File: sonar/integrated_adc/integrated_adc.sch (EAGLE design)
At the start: 0 parts

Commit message: Largely done schematic.
Still to do:
- Teensy-style connections
- Analog connections
- Remember what else I'm forgetting.
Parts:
- added C1, C2: 22pF, resistor:C-EUC0805
- added C10, C11, C12, C13, C3, C4, C5, C6, C7, C8, C9: 0u1, resistor:C-EUC0805
- added C14: 4u7, resistor:C-EUC0805
- added C15: 10n, resistor:C-EUC0805
- added C16: 1u, resistor:C-EUC0805
- added CON1, CON2: UAVCAN_MICRO, integrated_adc:UAVCAN_MICRO
- added JP1: CORTEX-M-DBG, integrated_adc:CORTEX-M-DBG
- added R1: 10K, resistor:R-EU_R0805
- added U$1: MCP3021, integrated_adc:MCP3021
- added U$2: MCP2562-E/SN, integrated_adc:MCP2562-E/SN
- added U1: STM32F303RX, integrated_adc:STM32F303RX
- added Y1: NX5032, integrated_adc:NX5032
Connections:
- new net !RST: JP1.!RESET, R1.1, U1G$5.NRST
- new net +3V3: C10.1, C11.1, C12.1, C13.1, C14.1, C3.1, C4.1, C5.1, C6.1, C7.1, C8.1, C9.1, JP1.VCC, R1.2, U$2.VDD, U$2.VIO, U1G$5.VDD
- new net +3V3_CLEAN: C15.1, C16.1, U$1.VDD, U1G$5.VDDA
- new net ADC1: U1G$1.PA0
- new net ADC2: U1G$1.PA4
- new net ADC3: U1G$2.PB13
- new net ADC4: U1G$2.PB14
- new net CAN_RX: U$2.RXD, U1G$1.PA11
- new net CAN_TX: U$2.TXD, U1G$1.PA12
- new net GND: C1.2, C10.2, C11.2, C12.2, C13.2, C14.2, C2.2, C3.2, C4.2, C5.2, C6.2, C7.2, C8.2, C9.2, JP1.GND_1, JP1.GND_2, JP1.GND_DETECT, U$2.STBY, U$2.VSS, U1G$5.BOOT0, U1G$5.VSS
- new net GNDA: C15.2, C16.2, U$1.VSS, U1G$5.VSSA
- new net I2C2_SCL: U1G$1.PA9
- new net I2C2_SDA: U1G$1.PA10
- new net N$1: C1.1, U1G$5.PF0/OSC-IN, Y1.2
- new net N$2: C2.1, U1G$5.PF1/OSC-OUT, Y1.1
- new net N$3: CON1.CANH, CON2.CANH, U$2.CANH
- new net N$4: CON1.CANL, CON2.CANL, U$2.CANL
- new net N$5: CON1.+5V, CON2.+5V
- new net N$6: CON1.GND, CON1.TABS, CON2.GND, CON2.TABS
- new net SCL: U$1.SCL
- new net SDA: U$1.SDA
- new net SWCLK: JP1.SWCLK/TCK
- new net SWDCLK: U1G$1.PA14
- new net SWDIO: JP1.SWDIO/TMS, U1G$1.PA13
- new net TRACESWO: JP1.SWO/TDO, U1G$2.PB3
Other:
- note added: "12MHz"
- note added: "22pF loading capacitors not verified for 12MHz!"
- note added: "ADC1_IN1"
- note added: "ADC2_IN1"
- note added: "ADC3_IN5"
- note added: "ADC4_IN4"
- note added: "CAN Bus"
- note added: "Clock and Power"
- note added: "Debug Header"
- note added: "Decoupling"
- note added: "External ADC"
- note added: "Pin Assignments"

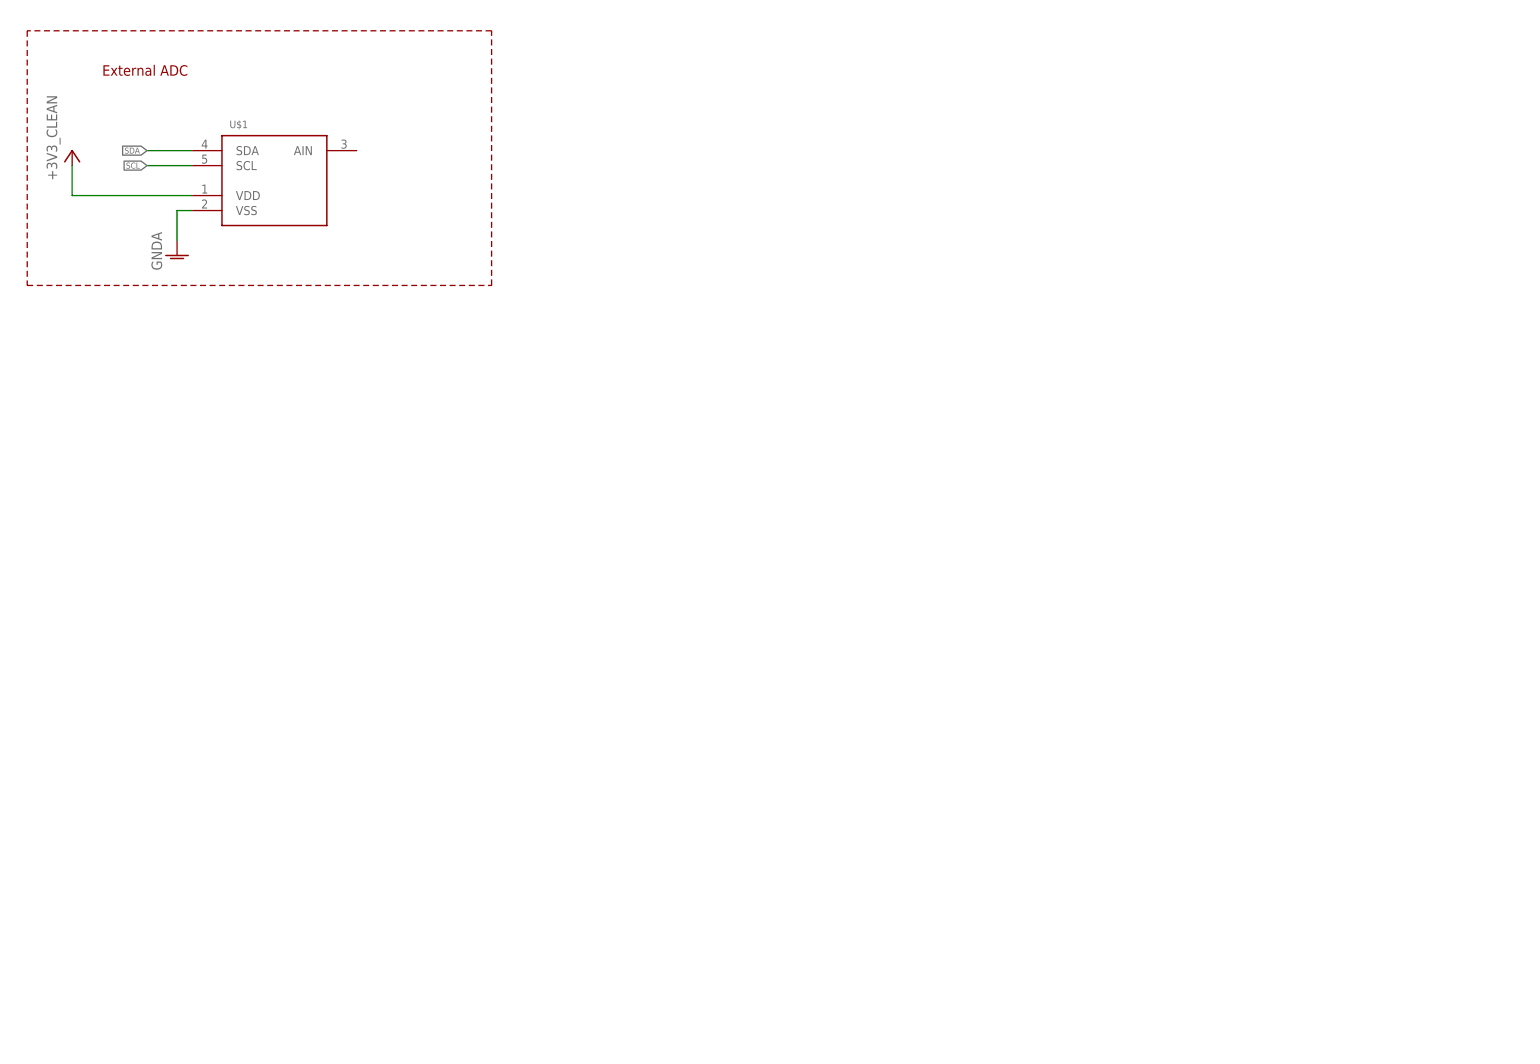
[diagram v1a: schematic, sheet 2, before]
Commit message: Switched to LQFP100 STM32 and added some headers.
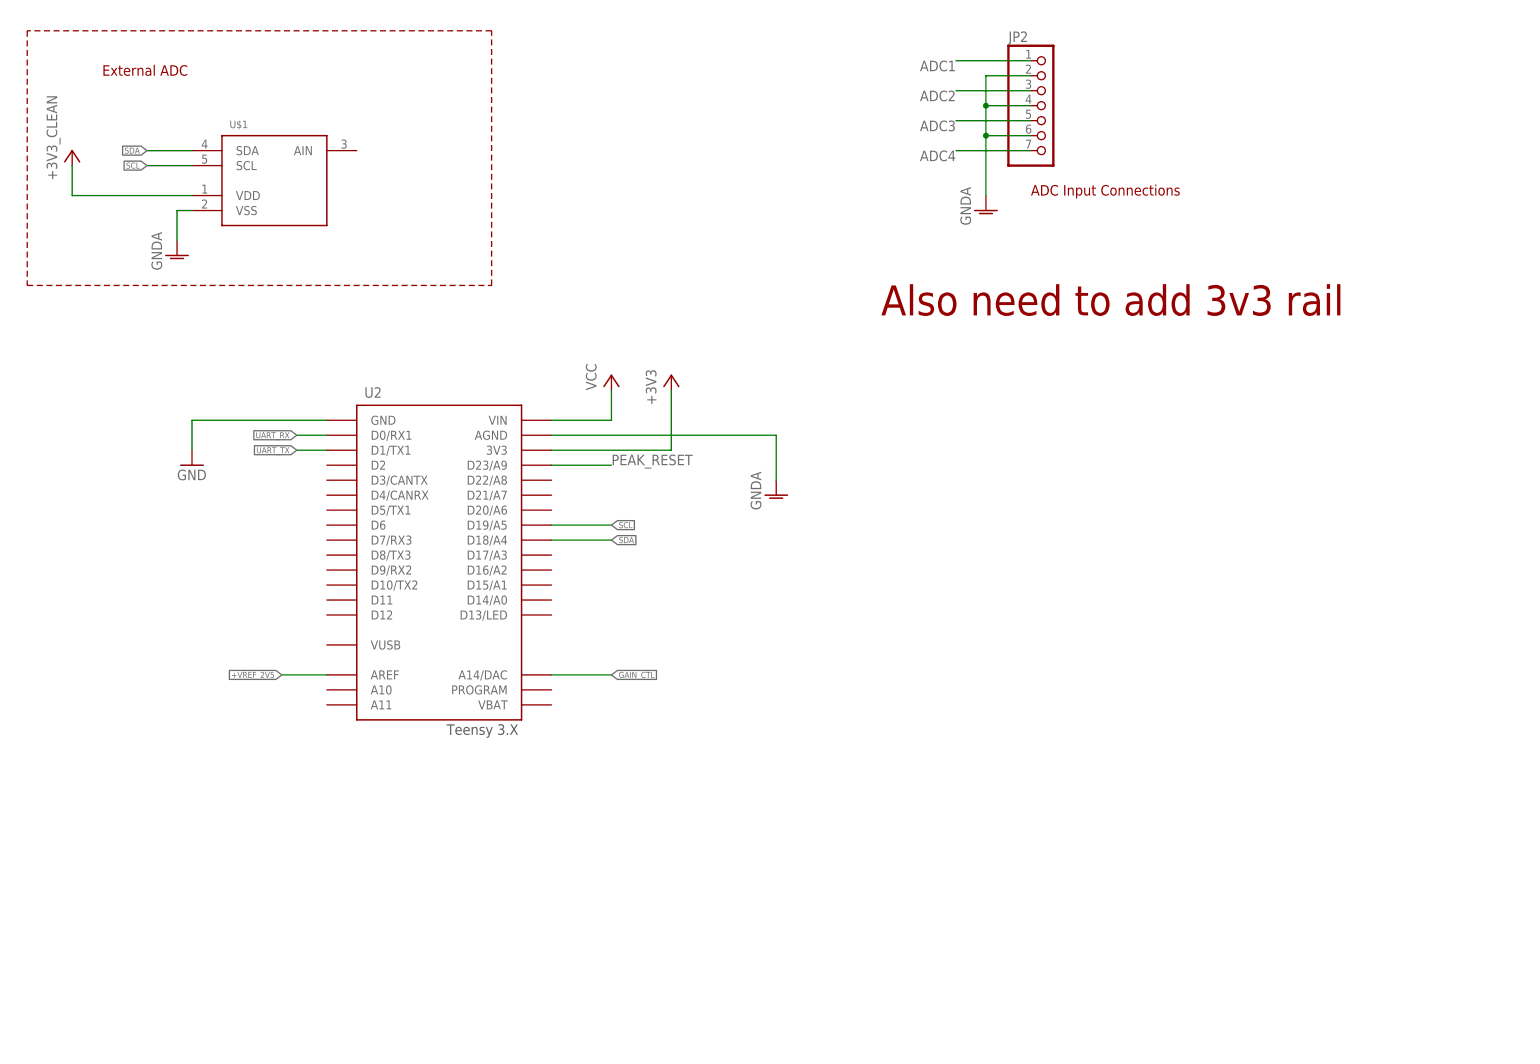
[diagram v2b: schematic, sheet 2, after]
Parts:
- removed U1: STM32F303RX, integrated_adc:STM32F303RX
- added JP2: (no value), pinhead:PINHD-1X7/90
- added U$3: STM32F303VE, integrated_adc:STM32F303VE
- added U2: TEENSY_3.X_PINOUT, integrated_adc:TEENSY_3.X_PINOUT
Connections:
- new net +VREF_2V5: U$3G$6.VREF+, U2.AREF
- new net GAIN_CTL: U2.A14/DAC
- new net N$7: U$3G$6.VSS
- new net PEAK_RESET: U2.D23/A9
- new net UART_RX: U2.D0/RX1
- new net UART_TX: U2.D1/TX1
- new net VCC: U2.VIN
- new net VREF: U$3G$6.VDDA
- net !RST: now also U$3G$6.NRST; no longer U1G$5.NRST
- net +3V3: now also U$3G$6.VDD, U2.3V3; no longer U1G$5.VDD
- net +3V3_CLEAN: no longer U1G$5.VDDA
- net ADC1: now also JP2.1, U$3G$1.PA0; no longer U1G$1.PA0
- net ADC2: now also JP2.3, U$3G$1.PA4; no longer U1G$1.PA4
- net ADC3: now also JP2.5, U$3G$2.PB13; no longer U1G$2.PB13
- net ADC4: now also JP2.7, U$3G$2.PB14; no longer U1G$2.PB14
- net CAN_RX: now also U$3G$1.PA11; no longer U1G$1.PA11
- net CAN_TX: now also U$3G$1.PA12; no longer U1G$1.PA12
- net GND: now also U$3G$6.BOOT0, U2.GND; no longer U1G$5.BOOT0, U1G$5.VSS
- net GNDA: now also JP2.2, JP2.4, JP2.6, U$3G$6.VSSA, U2.AGND; no longer U1G$5.VSSA
- net I2C2_SCL: now also U$3G$1.PA9; no longer U1G$1.PA9
- net I2C2_SDA: now also U$3G$1.PA10; no longer U1G$1.PA10
- net N$1: now also U$3G$6.PF0/OSC-IN; no longer U1G$5.PF0/OSC-IN
- net N$2: now also U$3G$6.PF1/OSC-OUT; no longer U1G$5.PF1/OSC-OUT
- net SCL: now also U2.D19/A5
- net SDA: now also U2.D18/A4
- net SWDCLK: now also U$3G$1.PA14; no longer U1G$1.PA14
- net SWDIO: now also U$3G$1.PA13; no longer U1G$1.PA13
- net TRACESWO: now also U$3G$2.PB3; no longer U1G$2.PB3
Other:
- note added: "ADC Input Connections"
- note added: "Also need to add 3v3 rail"
- note added: "Verify Pinouts again."

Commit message: Theoretically done schematic.
Need to verify again later when I have a fresh brain.
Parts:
- added C17: 10n, resistor:C-EUC0805
- added C18: 1u, resistor:C-EUC0805
- added R2, R3: (no value), resistor:R-EU_R0805
- added U$4: AMPHENOL_MICROB-USB, integrated_adc:AMPHENOL_MICROB-USB
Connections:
- net N$1 renamed OSC_IN
- net N$2 renamed OSC_OUT
- net N$3 renamed CANH
- net N$4 renamed CANL
- removed net I2C2_SCL: U$3G$1.PA9
- removed net I2C2_SDA: U$3G$1.PA10
- removed net VREF: U$3G$6.VDDA
- new net +5V: U$2.VDD
- new net GPIO_0: U2.D8/TX3
- new net GPIO_1: U2.D9/RX2
- new net GPIO_2: U2.D10/TX2
- new net GPIO_3: U2.D11
- new net GPIO_4: U2.D12
- new net PEAK_SIG: U2.D22/A8
- new net USB_D+: R3.2, U$4.D+
- new net USB_D-: R2.2, U$4.D-
- new net USB_DM: R2.1, U$3G$1.PA11
- new net USB_DP: R3.1, U$3G$1.PA12
- net +3V3: now also C15.1, C16.1, U$3G$6.VDDA; no longer U$2.VDD
- net +3V3_CLEAN: no longer C15.1, C16.1
- net +VREF_2V5: now also C17.1, C18.1
- net CAN_RX: now also U$3G$2.PB8; no longer U$3G$1.PA11
- net CAN_TX: now also U$3G$2.PB9; no longer U$3G$1.PA12
- net GND: now also C15.2, C16.2, U$4.GND, U$4.TABS
- net GNDA: now also C17.2, C18.2; no longer C15.2, C16.2
- net SCL: now also U$3G$1.PA9
- net SDA: now also U$3G$1.PA10
- net UART_RX: now also U$3G$4.PD9
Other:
- note added: "+VBUS shouldn't be connected. According to spec, ID should be disconnected if it is a device."
- note added: "Analog Reference"
- note added: "From SiLabs app note: - Route as short as possible - 90 ohm impedance - 15 ohm serial resistors on D+/D-"
- note added: "I2C2"
- note added: "Important Signals from the Preprocessor - D23: Peak detector reset - D22: peak detector signal - D14: Gain control positive input - D1: UART TX - D0: UART RX - D18: SDA - D19: SCL - AREF: 2.5V analog reference"
- note added: "USART3"

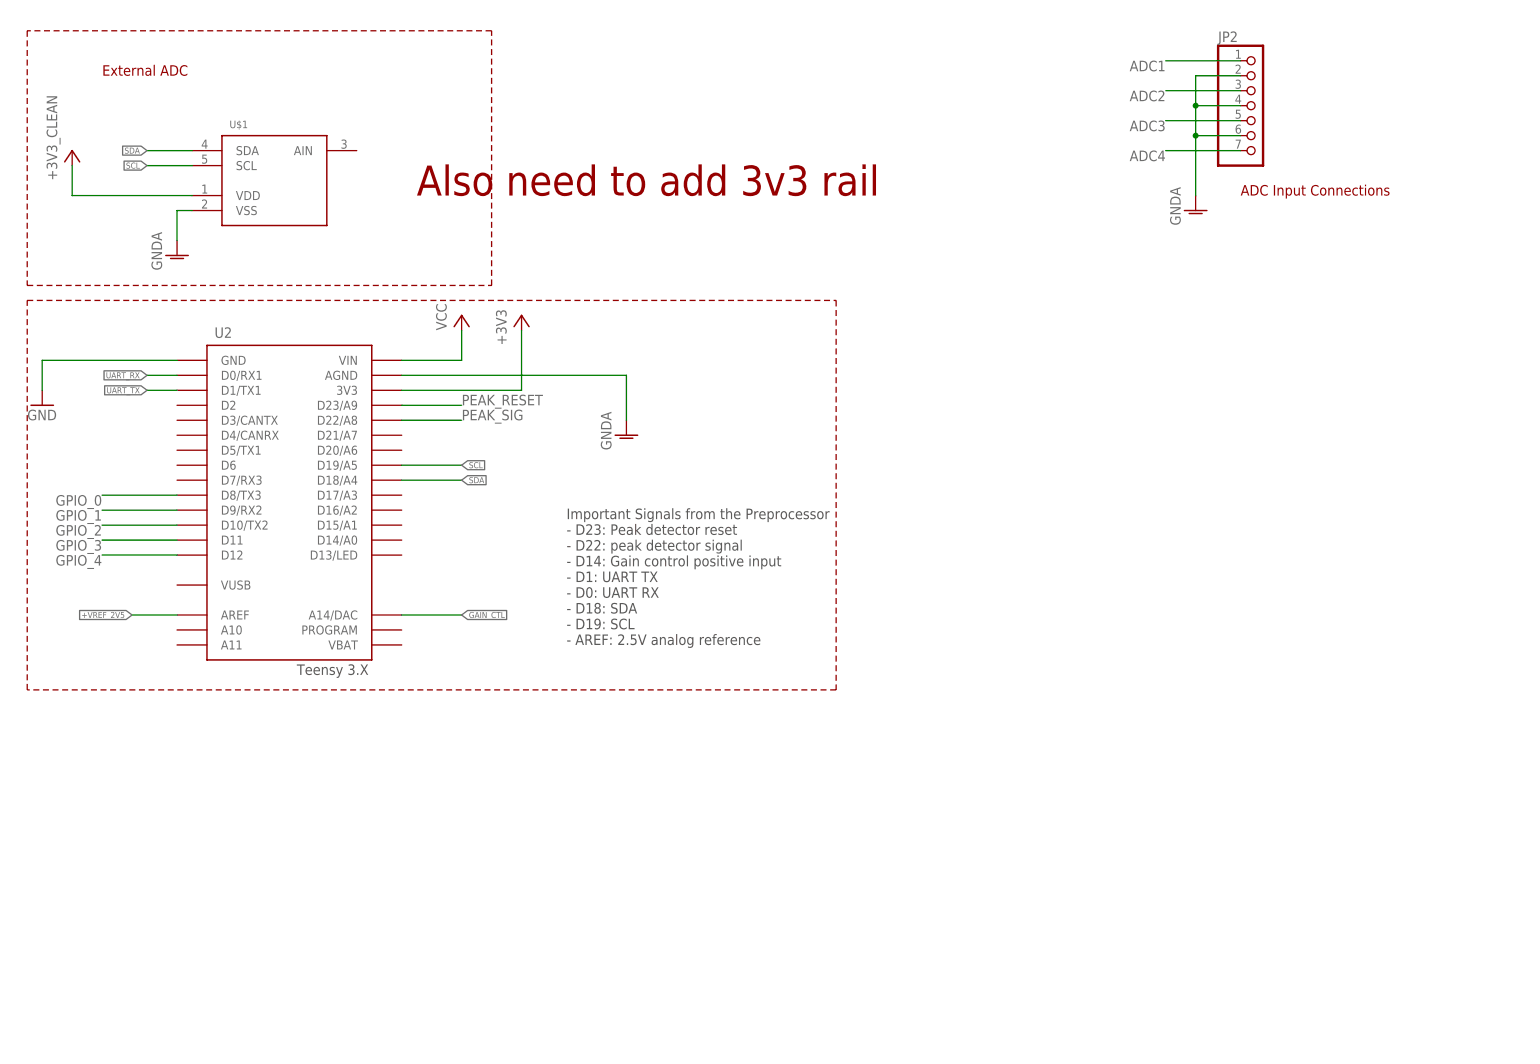
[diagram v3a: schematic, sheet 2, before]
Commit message: Schematic is probably done for real now.
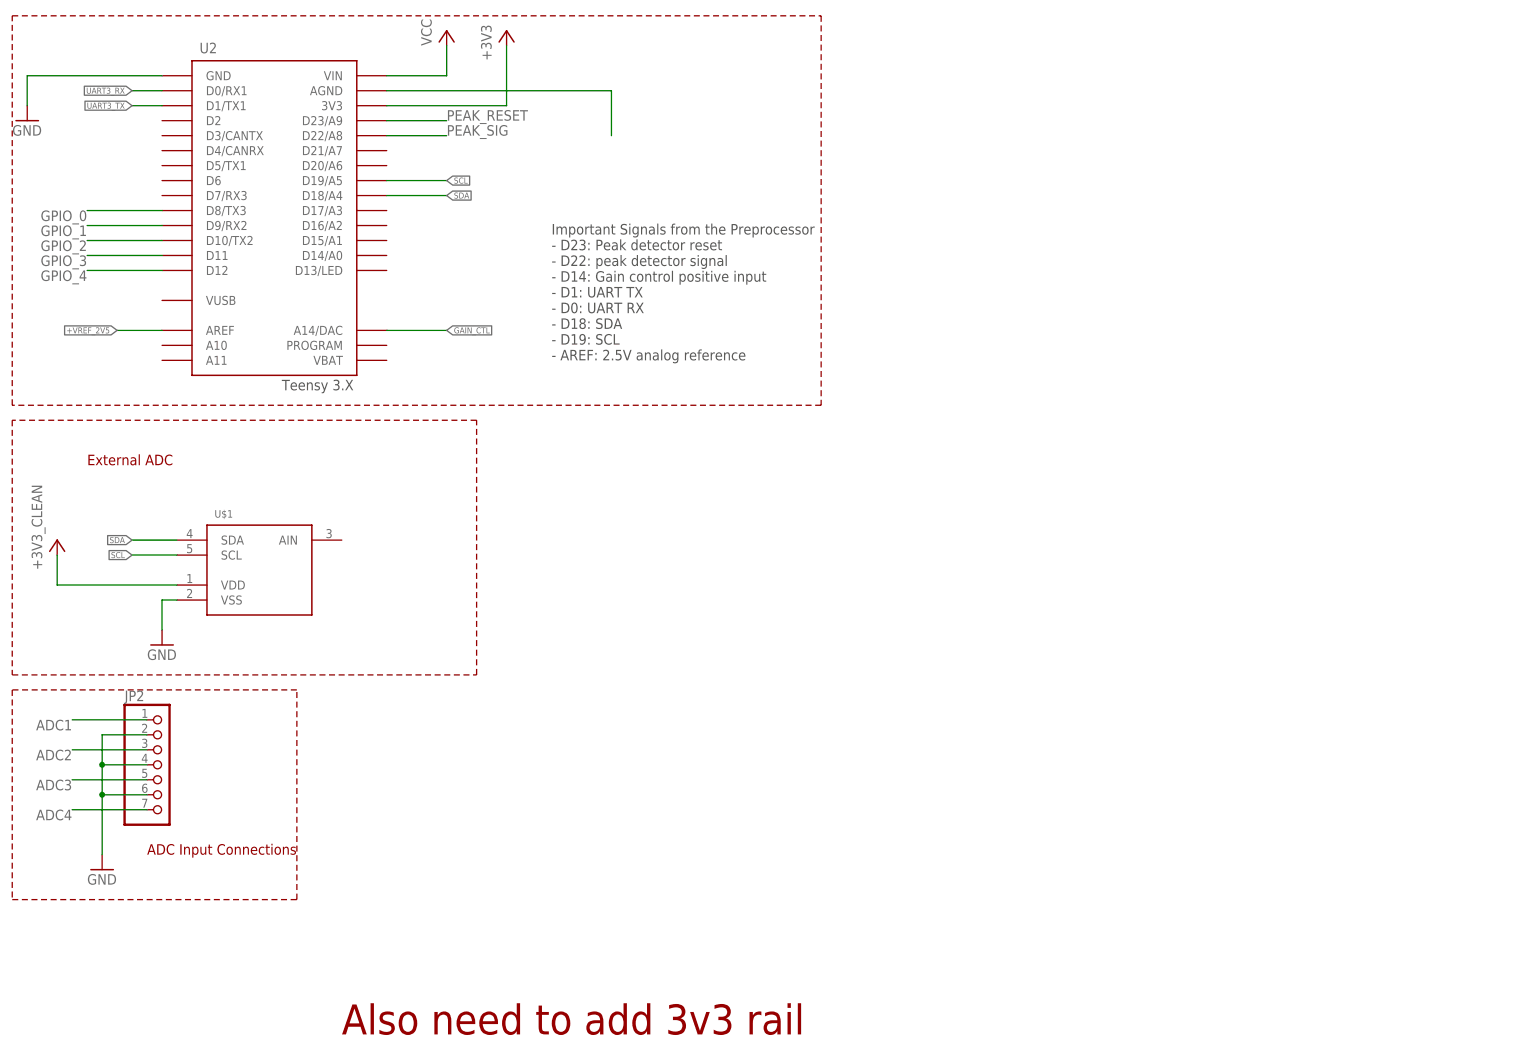
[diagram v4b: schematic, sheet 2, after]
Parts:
- added JP3: (no value), pinhead:PINHD-1X6/90
- added U1: AP2112K-3.3TRG1, integrated_adc:AP2112K-3.3TRG1
- R2, R3: value (none) -> 15
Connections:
- net UART_RX renamed UART3_RX
- removed net GNDA: C17.2, C18.2, JP2.2, JP2.4, JP2.6, U$1.VSS, U$3G$6.VSSA, U2.AGND
- removed net UART_TX: U2.D1/TX1
- new net N$2: JP3.2
- new net N$3: JP3.3
- new net N$8: U2.AGND
- new net N$9: JP3.6
- new net UART1_RX: JP3.5, U$3G$2.PB7
- new net UART1_TX: JP3.4, U$3G$2.PB6
- new net UART3_TX: U$3G$4.PD8, U2.D1/TX1
- net +3V3: now also U1.VOUT
- net GND: now also C17.2, C18.2, JP2.2, JP2.4, JP2.6, JP3.1, U$1.VSS, U$3G$6.VSSA, U1.GND
- net VCC: now also U1.EN, U1.VIN
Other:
- note added: "All UART pins are 5V tolerant."
- note added: "Digital Supply"
- note added: "Extra UART pinout. Meant to mate with those FTDI usb dongles."
- note added: "USB"
- note added: "Used to have seperate analog and digital ground, but on further research that isn't necessarily the best idea. Split grounds can "force" return paths in weird ways, so it's generally a better idea to just do careful routing."
- note removed: "USART3"
- moved on the sheet: JP2, R2, R3, U$1, U2
